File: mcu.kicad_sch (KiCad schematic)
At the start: 4 parts, among them J1 2171750001, U1 STM32G473CEUx

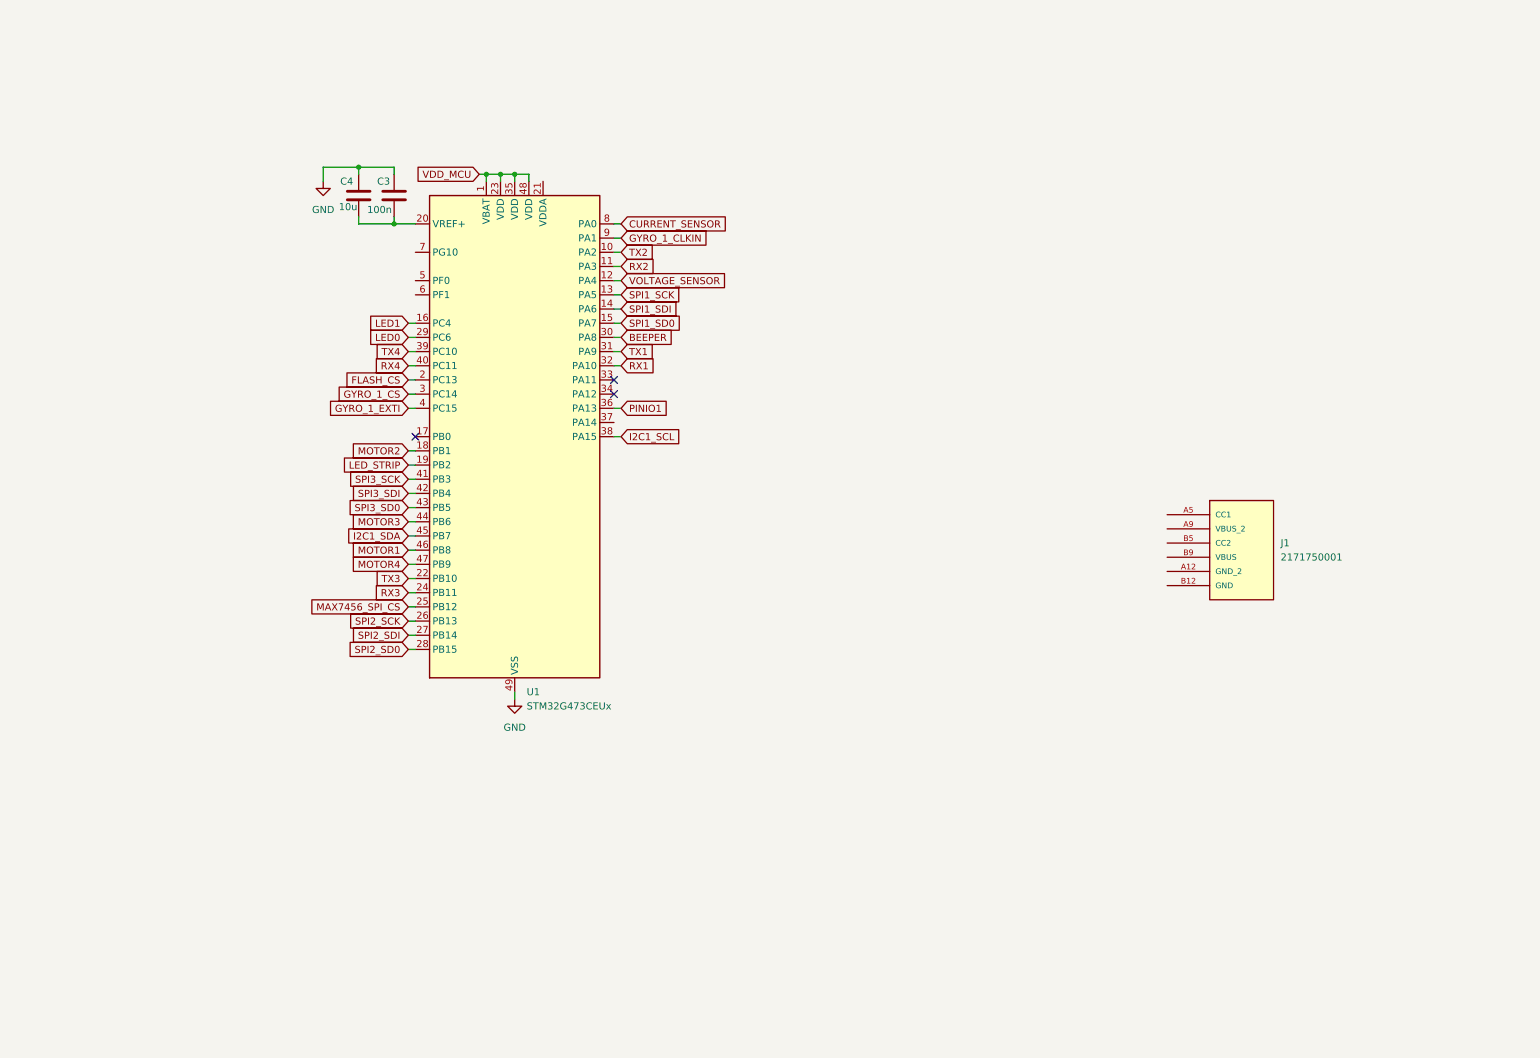
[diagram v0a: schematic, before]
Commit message: Refactor sensor.kicad_sch: Adjust component positions and update property attributes for ICM-42688-P
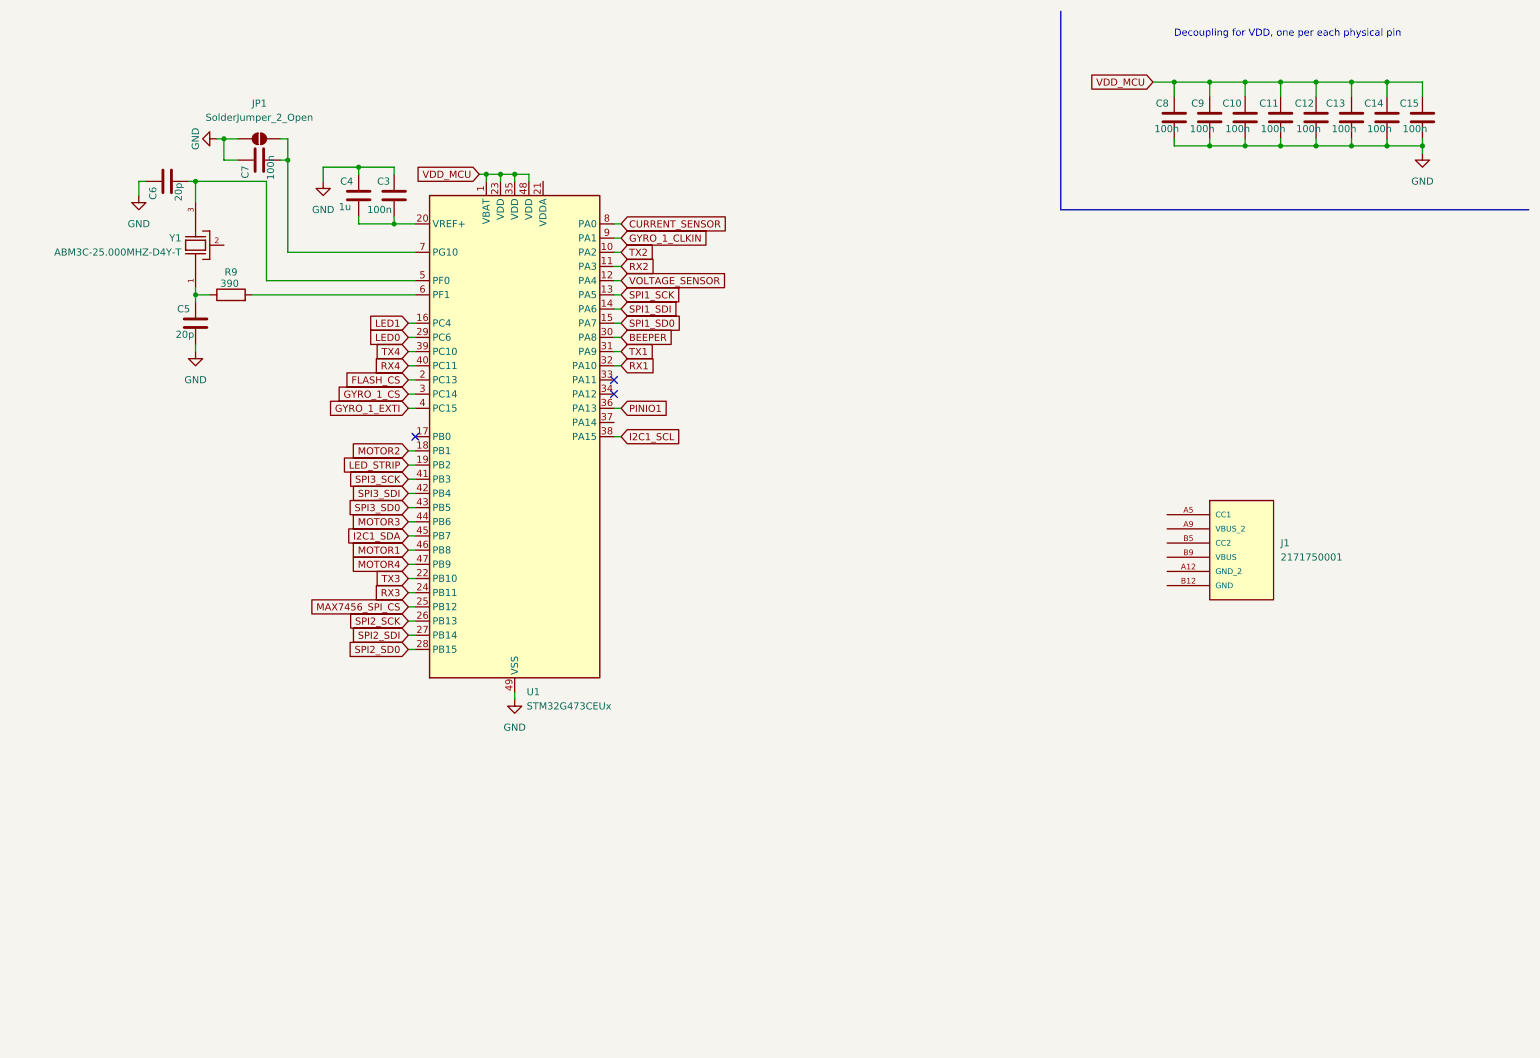
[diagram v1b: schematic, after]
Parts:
- added C10, C11, C12, C13, C14, C15, C7, C8, C9: 100n, symbol Device:C
- added C5, C6: 20p, symbol Device:C
- added JP1: SolderJumper_2_Open, symbol Jumper:SolderJumper_2_Open
- added R9: 390, symbol Device:R
- added Y1: ABM3C-25.000MHZ-D4Y-T, fcg4_fp:XTAL_ABM3C-25.000MHZ-D4Y-T, symbol fcg4:ABM3C-25.000MHZ-D4Y-T
- C4: value 10u -> 1u
- J1: footprint 2171750001:2171750001_MOL -> fcg4_fp:2171750001_MOL
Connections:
- net GND: now also C10.2, C11.2, C12.2, C13.2, C14.2, C15.2, C5.2, C6.1, C7.1, C8.2, C9.2, JP1.1 (A)
- net VDD_MCU: now also C10.1, C11.1, C12.1, C13.1, C14.1, C15.1, C8.1, C9.1
- net at U1.5 (PF0): now also C6.2, Y1.3
- net at U1.6 (PF1): now also R9.2
- net at U1.7 (PG10): now also C7.2, JP1.2 (B)
- new net: C5.1, R9.1, Y1.1
- new net: Y1.2, Y1.4
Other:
- note added: "Decoupling for VDD, one per each physical pin"

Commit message: Refactor code structure for improved readability and maintainability
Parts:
- removed J1: 2171750001, fcg4_fp:2171750001_MOL, symbol fcg4:2171750001
- added J1: USB4105-GF-A-120, fcg4_fp:GCT_USB4105-GF-A-120, symbol fcg4:USB4105-GF-A-120
- added R10, R11: 5k1, symbol Device:R
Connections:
- net GND: now also J1.A1_B12 (GND), J1.SH1 (SHELL_GND), R10.1, R11.1
- new net: J1.A5 (CC1), R10.2
- new net: J1.B5 (CC2), R11.2
- new net 5V8USB: J1.A4_B9 (VBUS)
- new net DIFF+: J1.A6 (DP1), J1.B6 (DP2)
- new net DIFF-: J1.A7 (DN1), J1.B7 (DN2)
- no-connect marks 3 -> 5

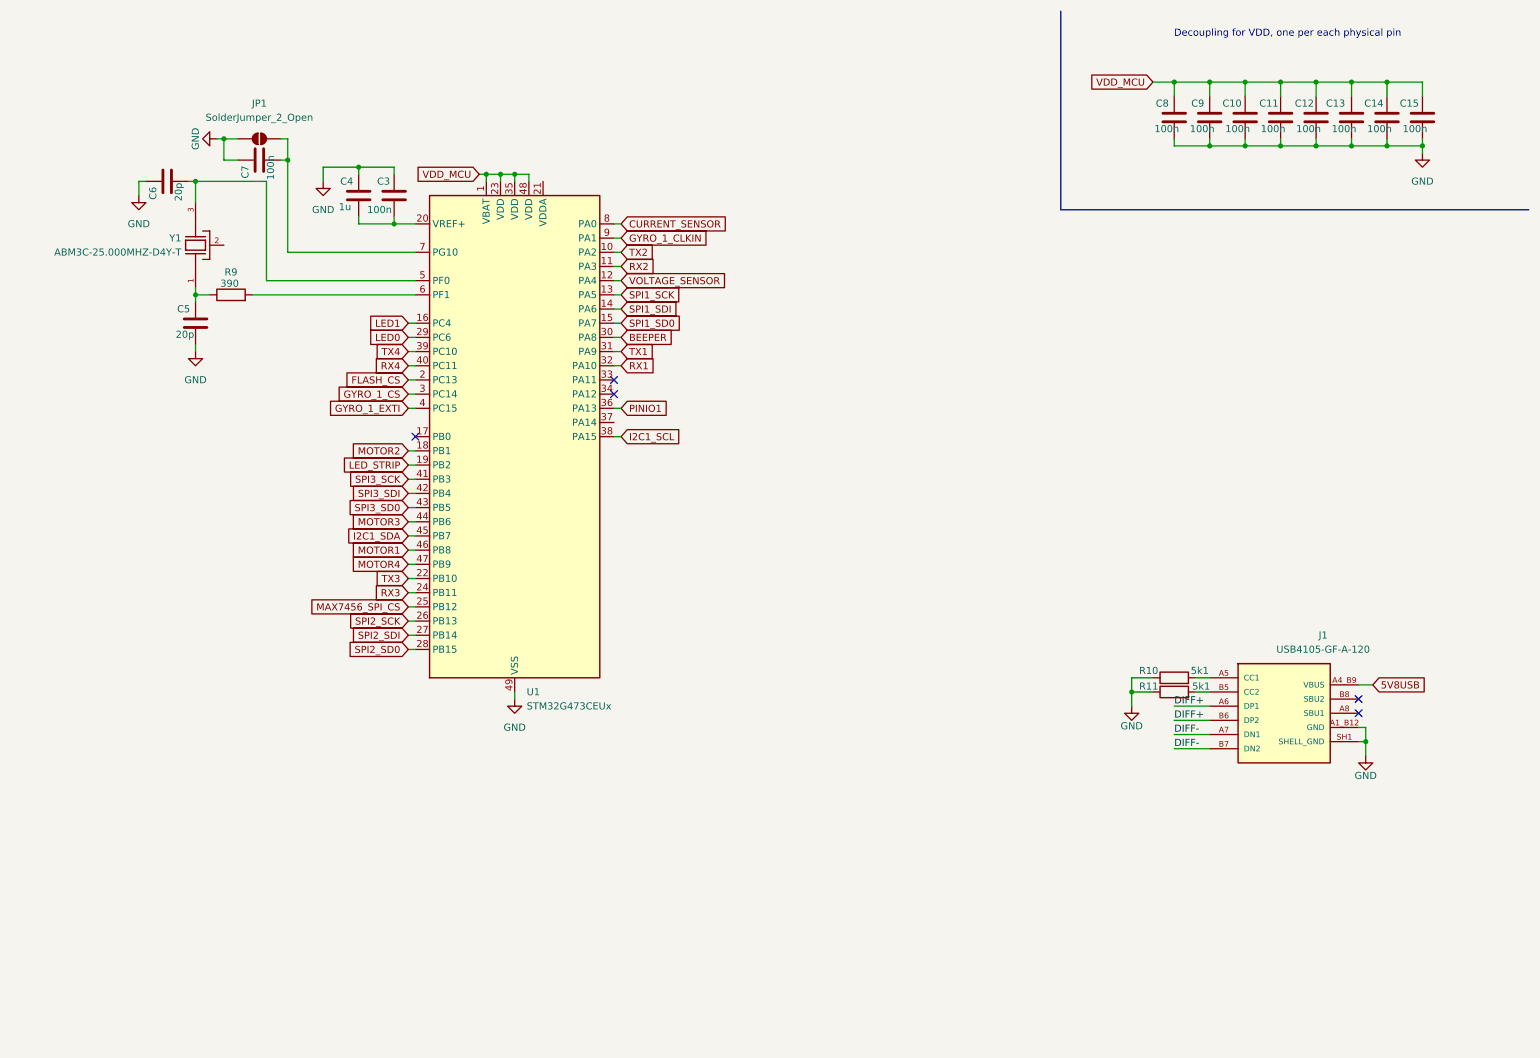
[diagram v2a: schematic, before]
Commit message: add sensors schematic
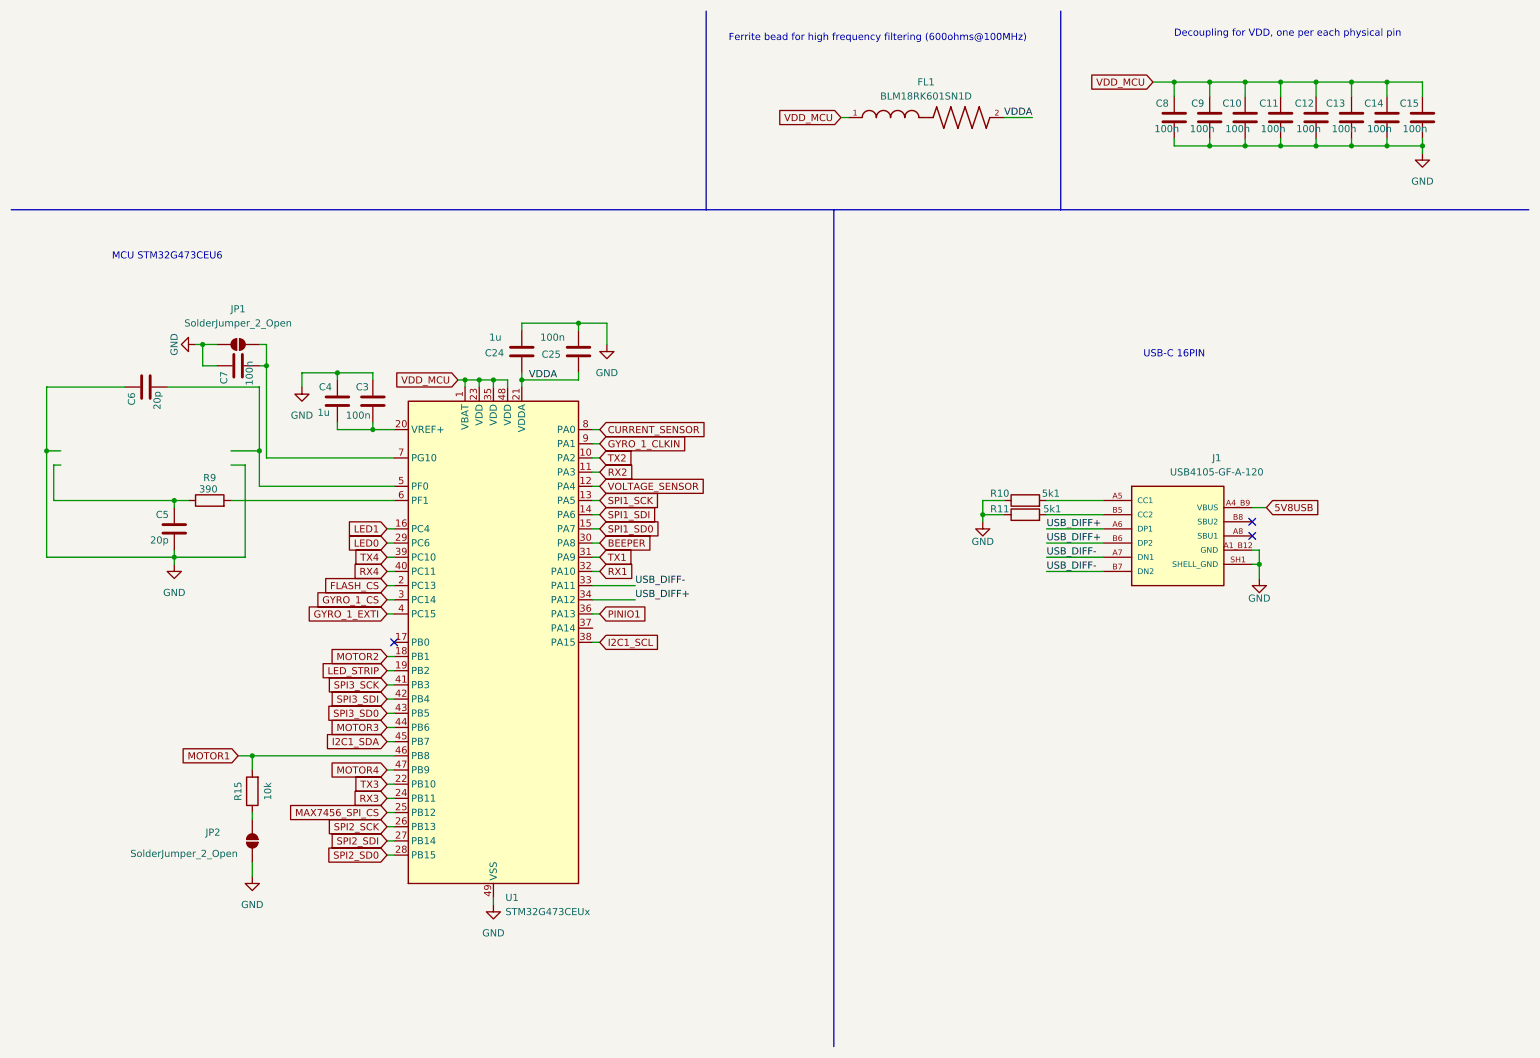
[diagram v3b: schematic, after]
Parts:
- removed Y1: ABM3C-25.000MHZ-D4Y-T, fcg4_fp:XTAL_ABM3C-25.000MHZ-D4Y-T, symbol fcg4:ABM3C-25.000MHZ-D4Y-T
- added C24: 1u, symbol Device:C
- added C25: 100n, symbol Device:C
- added FL1: BLM18RK601SN1D, fcg4_fp:BEADC1608X95N, symbol fcg4:BLM18RK601SN1D
- added JP2: SolderJumper_2_Open, symbol Jumper:SolderJumper_2_Open
- added R15: 10k, symbol Device:R
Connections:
- net DIFF+ is gone; now on net USB_DIFF+: J1.A6 (DP1), J1.B6 (DP2)
- net DIFF- is gone; now on net USB_DIFF-: J1.A7 (DN1), J1.B7 (DN2)
- net GND: now also C24.1, C25.1, JP2.1 (A)
- net MOTOR1: now also R15.2
- net VDD_MCU: now also FL1.1
- net VDDA: now reaches U1.21 (VDDA)
- net VDDA: now also C24.2, C25.2, FL1.2
- net USB_DIFF-: now reaches U1.33 (PA11)
- net USB_DIFF+: now reaches U1.34 (PA12)
- new net: JP2.2 (B), R15.1
- no-connect marks 5 -> 3
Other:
- note added: "Ferrite bead for high frequency filtering (600ohms@100MHz)"
- note added: "MCU STM32G473CEU6"
- note added: "USB-C 16PIN"
- moved on the sheet: C3, C4, C5, C6, C7, J1, JP1, R10, R11, R9, U1

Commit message: add wiring to soldering pads for uart, dji, and esc
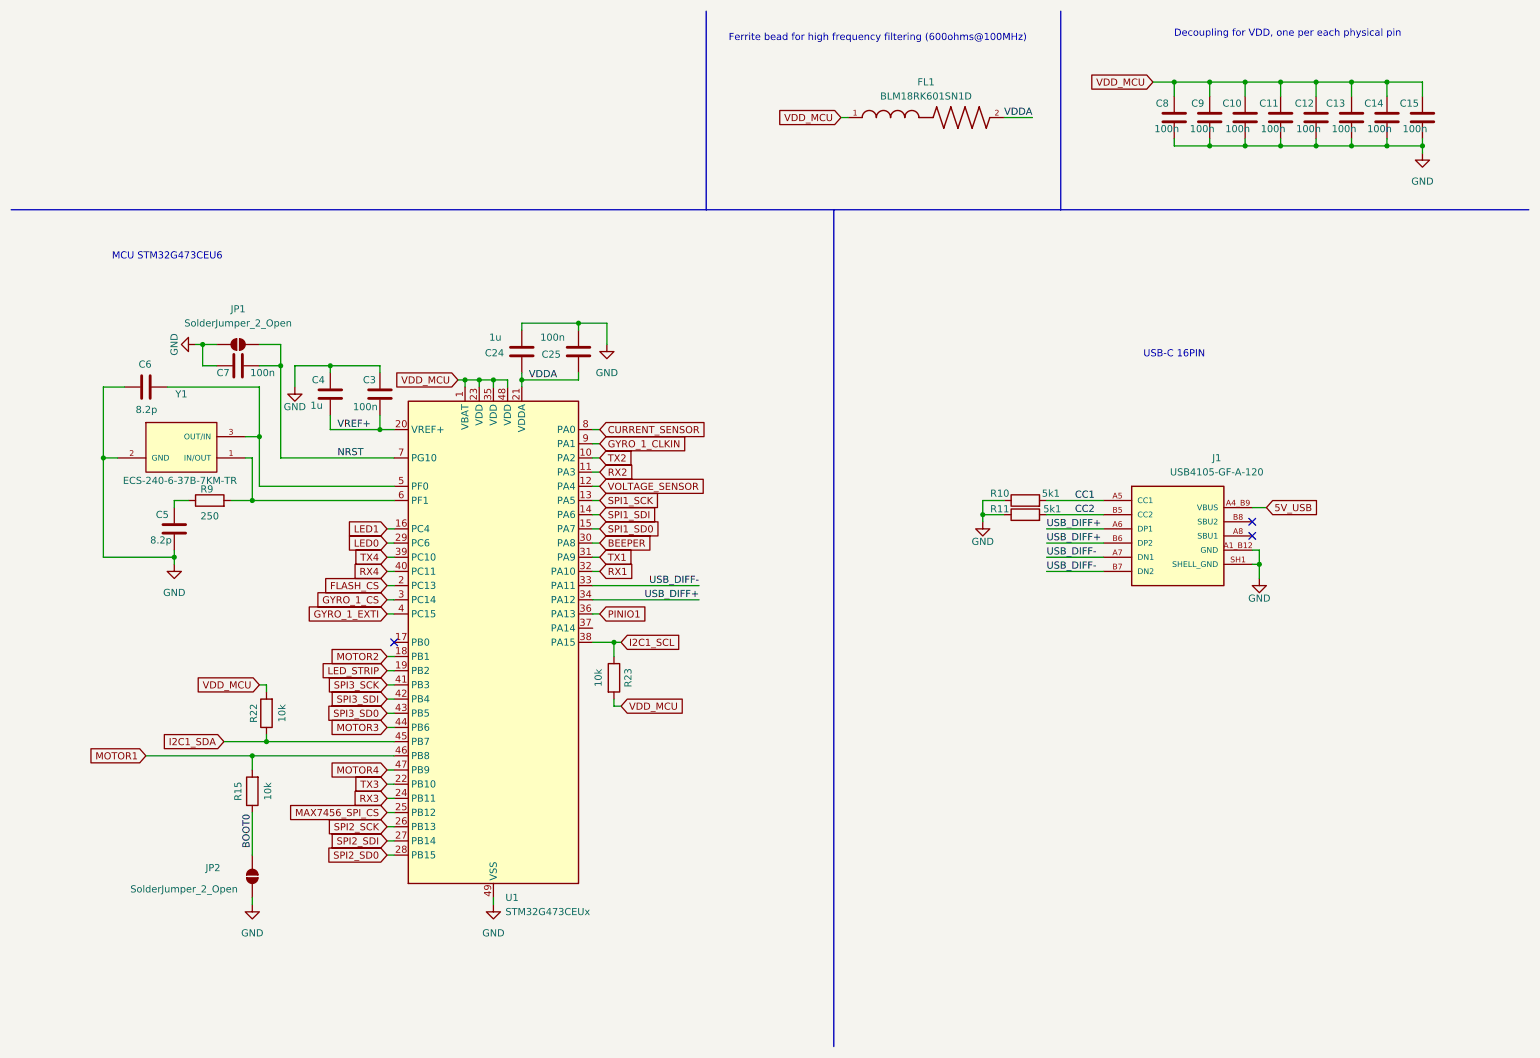
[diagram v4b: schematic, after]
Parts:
- added R22, R23: 10k, symbol Device:R
- added Y1: ECS-240-6-37B-7KM-TR, fcg4_fp:XTAL_ECS-240-6-37B-7KM-TR, symbol fcg4:ECS-240-6-37B-7KM-TR
- C5, C6: value 20p -> 8.2p
- R9: value 390 -> 250
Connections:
- net GND: now also Y1.2 (GND)
- net I2C1_SCL: now also R23.1
- net I2C1_SDA: now also R22.1
- net VDD_MCU: now also R22.2, R23.2
- net VREF+: now reaches C3.2, C4.2, U1.20 (VREF+)
- net at C6.2, U1.5 (PF0): now also Y1.3 (OUT/IN)
- net at R9.2, U1.6 (PF1): now also Y1.1 (IN/OUT)
- net NRST: now reaches C7.2, JP1.2 (B), U1.7 (PG10)
- net BOOT0: now reaches JP2.2 (B), R15.1
- net CC1: now reaches J1.A5 (CC1), R10.2
- net CC2: now reaches J1.B5 (CC2), R11.2
- net 5V8USB renamed 5V_USB
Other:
- moved on the sheet: C3, C4, JP2

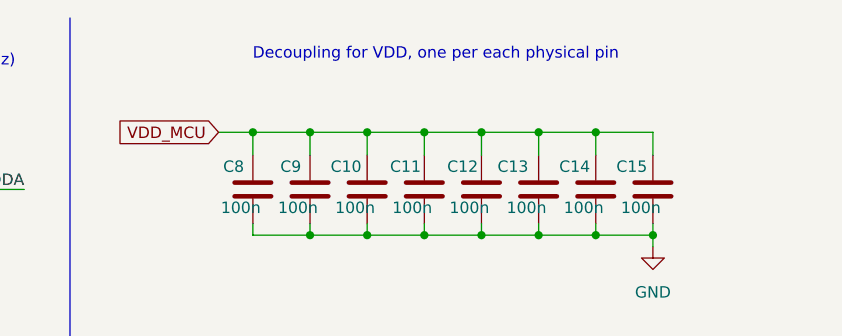
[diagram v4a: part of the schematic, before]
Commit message: - Removed SBUS receiver support in uart1 and added esc telemetry in uart2 - Added a new Mounting Hole symbol with properties and graphical representation in the schematic (fcg4.kicad_sch). (MountingHoles_30.5x30.5mm_Standard.kicad_mod) with appropriate pads and attributes. - Started PCB editor
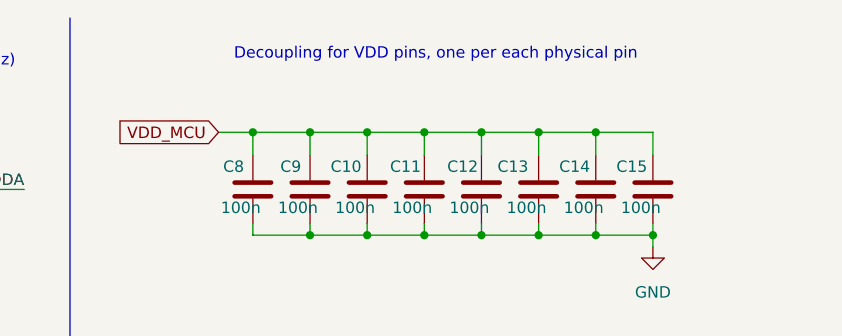
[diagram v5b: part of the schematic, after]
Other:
- note added: "Decoupling for VDD pins, one per each physical pin"
- note removed: "Decoupling for VDD, one per each physical pin"
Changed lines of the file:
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@@
 		)
 	)
-	(text "Decoupling for VDD, one per each physical pin"
+	(text "Decoupling for VDD pins, one per each physical pin"
 		(exclude_from_sim no)
 		(at 241.3 16.764 0)
